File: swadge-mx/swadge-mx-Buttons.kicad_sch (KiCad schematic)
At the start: 8 parts, among them SW1 YTS-D003-1A, SW2 YTS-D003-1A, SW3 YTS-D003-1A, SW4 YTS-D003-1A, SW5 YTS-D003-1A, SW6 YTS-D003-1A, SW7 B3FS-4002P, SW8 B3FS-4002P

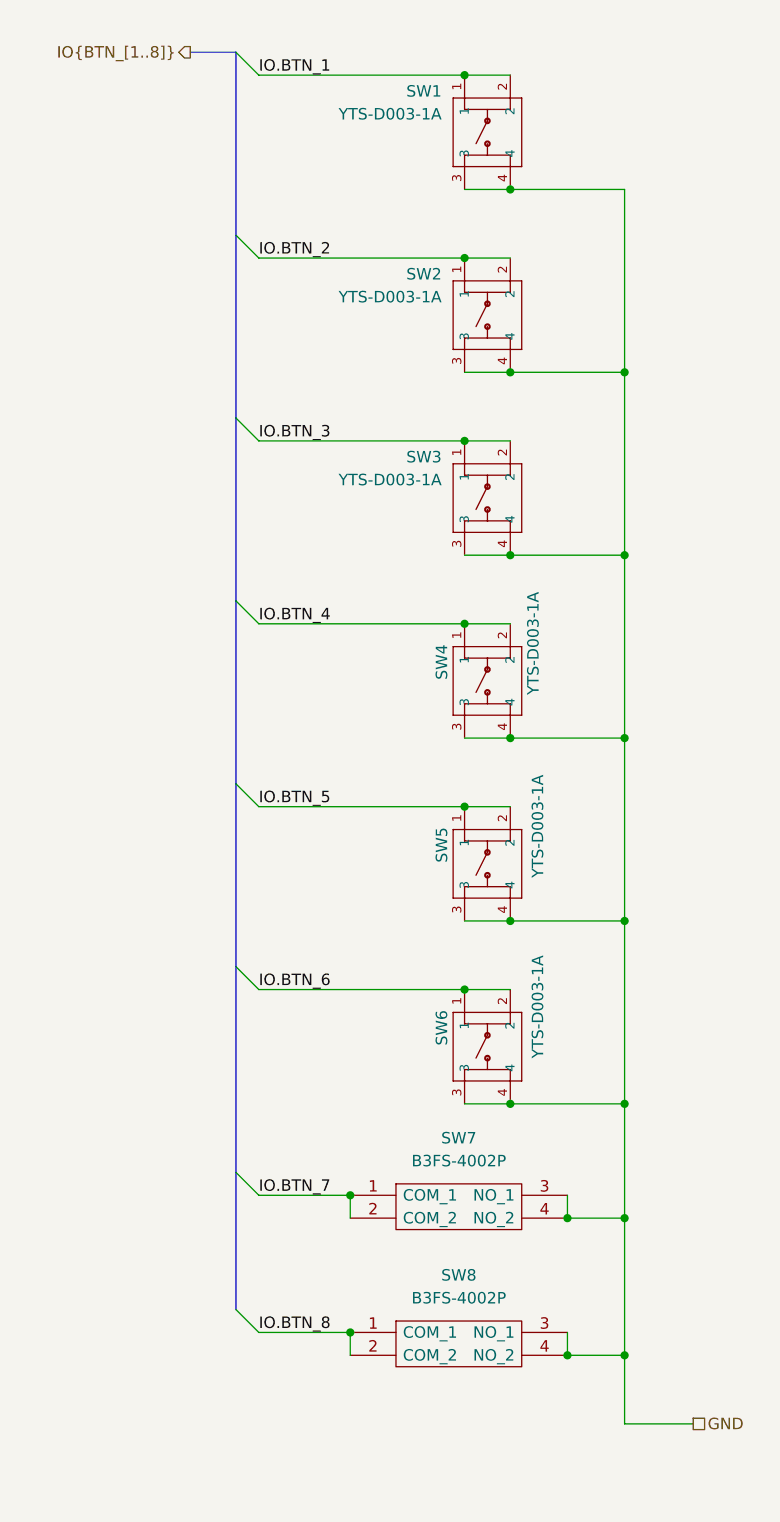
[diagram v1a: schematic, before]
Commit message: #4 Normalize button symbols, fix J8 attributes
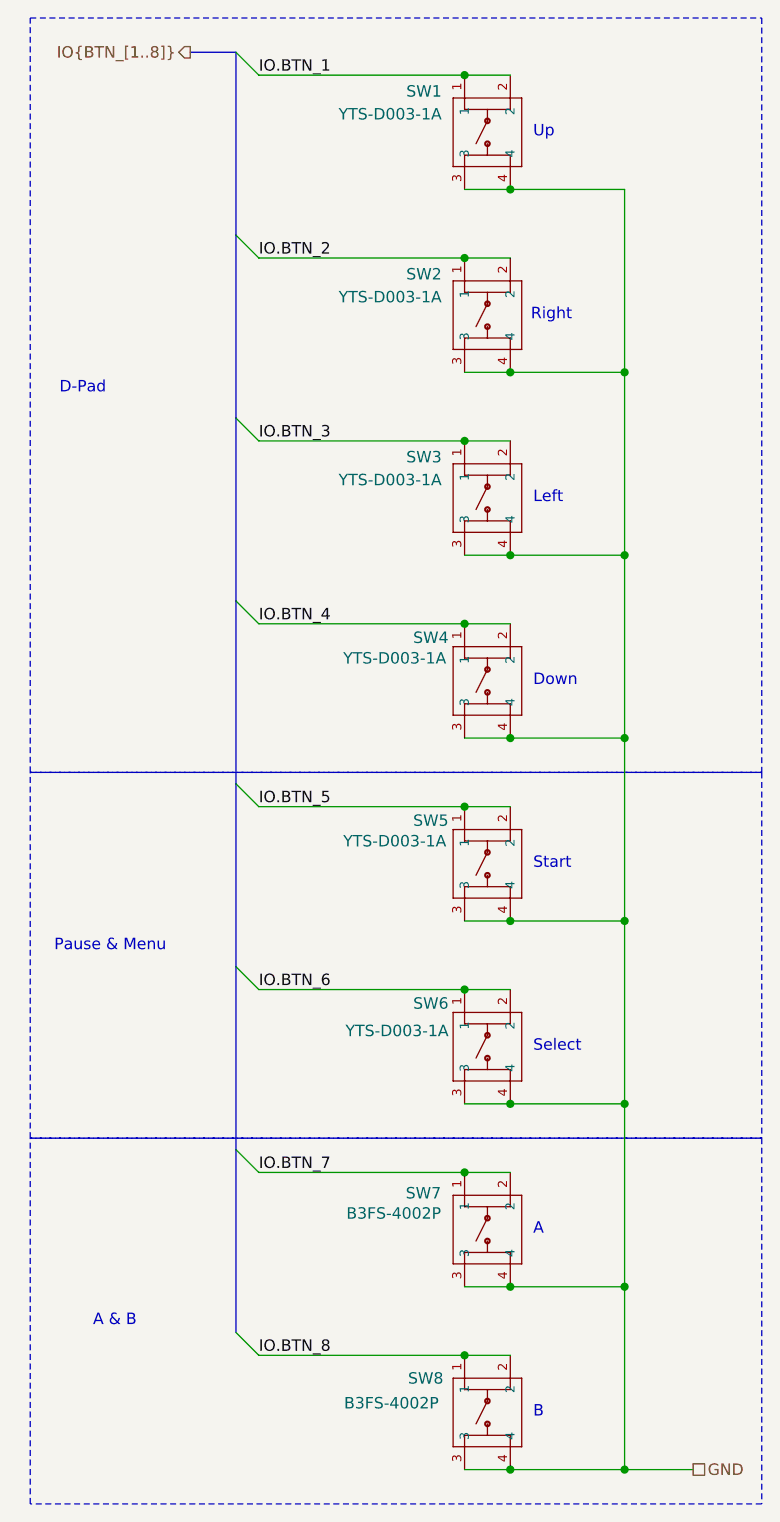
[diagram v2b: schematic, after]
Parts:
- SW7, SW8: Cost @ 2.5k 0.0461 -> (none); Cost100 76 -> (none); Cost@2500 (none) -> 0.0478
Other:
- note added: "A"
- note added: "A & B"
- note added: "B"
- note added: "D-Pad"
- note added: "Down"
- note added: "Left"
- note added: "Pause & Menu"
- note added: "Right"
- note added: "Select"
- note added: "Start"
- note added: "Up"
